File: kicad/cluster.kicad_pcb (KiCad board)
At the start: 2 copper layers, 24.5 x 36.5 mm, 17 parts, among them J1 Conn_01x07

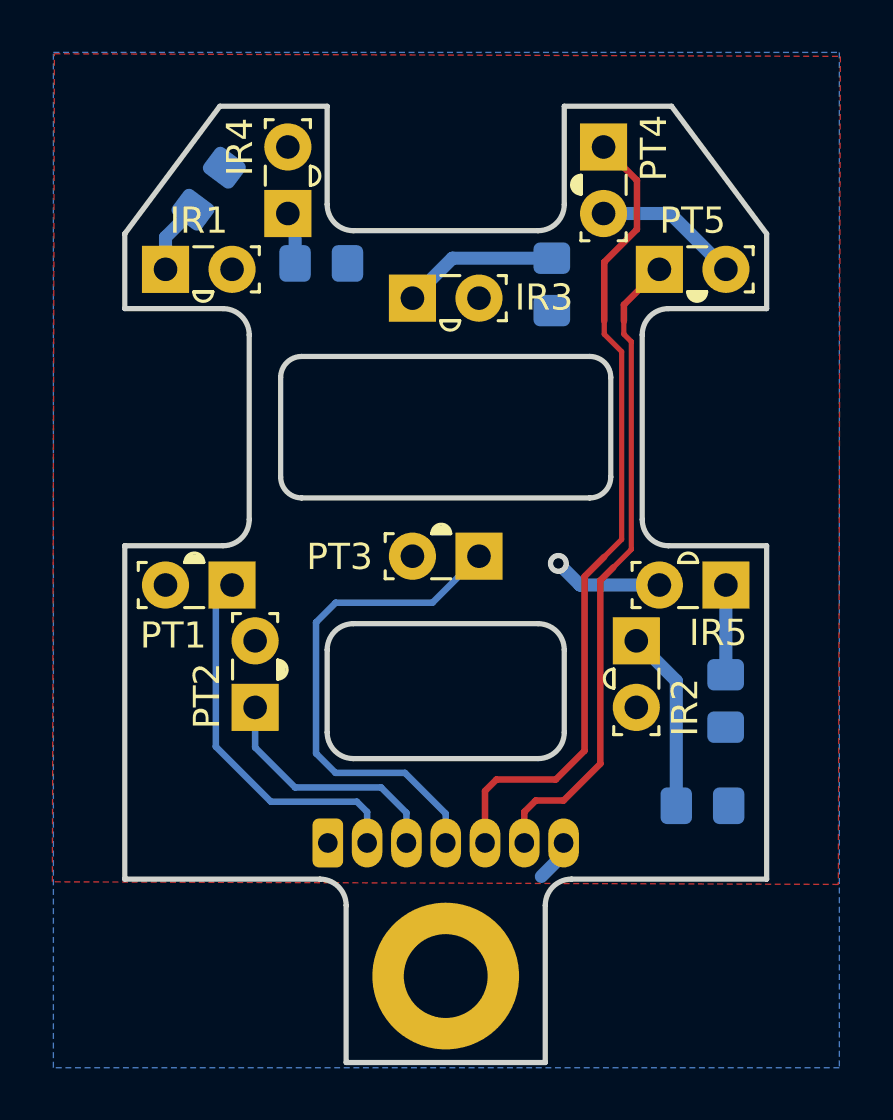
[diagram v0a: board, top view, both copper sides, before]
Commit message: Cluster pcb v2.5.1
- Make the slot for the center key wider, to avoid the nickel strip
catching on the edge when pressing the center key
- Fix the PT/LED placements for the north keywell. They were very
slightly offset from where they should be
- Minor component/trace placement changes, due to the widened center
key slot
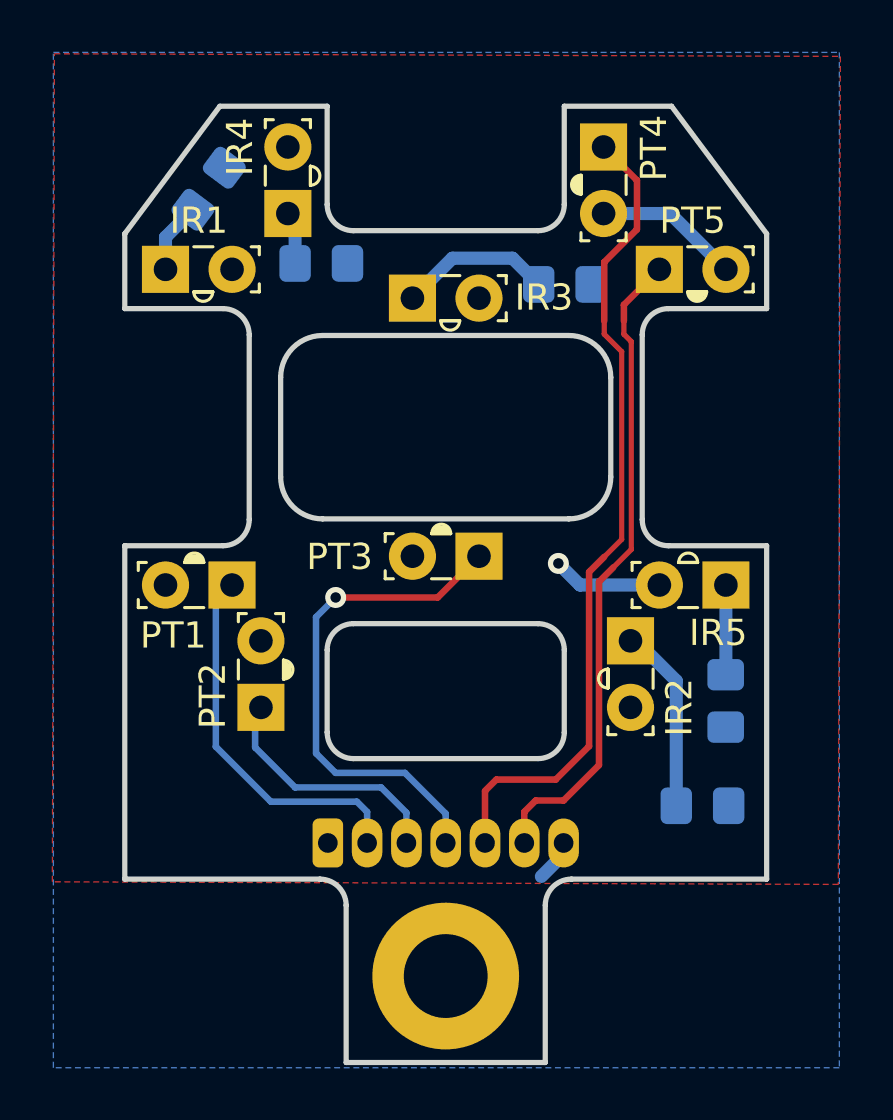
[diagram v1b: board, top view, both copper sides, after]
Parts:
- moved R3 0.50 mm to (167.0, 70.1), turned to 180 degrees
- moved IR2 0.22 mm to (169.5, 83.7)
- moved PT2 0.22 mm to (155.4, 86.2)
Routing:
- net C3: track 19.3 -> 19.8 mm, vias 0 -> 1
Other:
- outline, holes or cut-outs redrawn
- board text added: "v2.5.1"
- board text removed: "v2.5.0"
